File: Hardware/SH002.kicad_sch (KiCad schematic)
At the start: 11 parts, among them J3 Conn_01x04, J5 Conn_01x04, J7 Conn_01x04

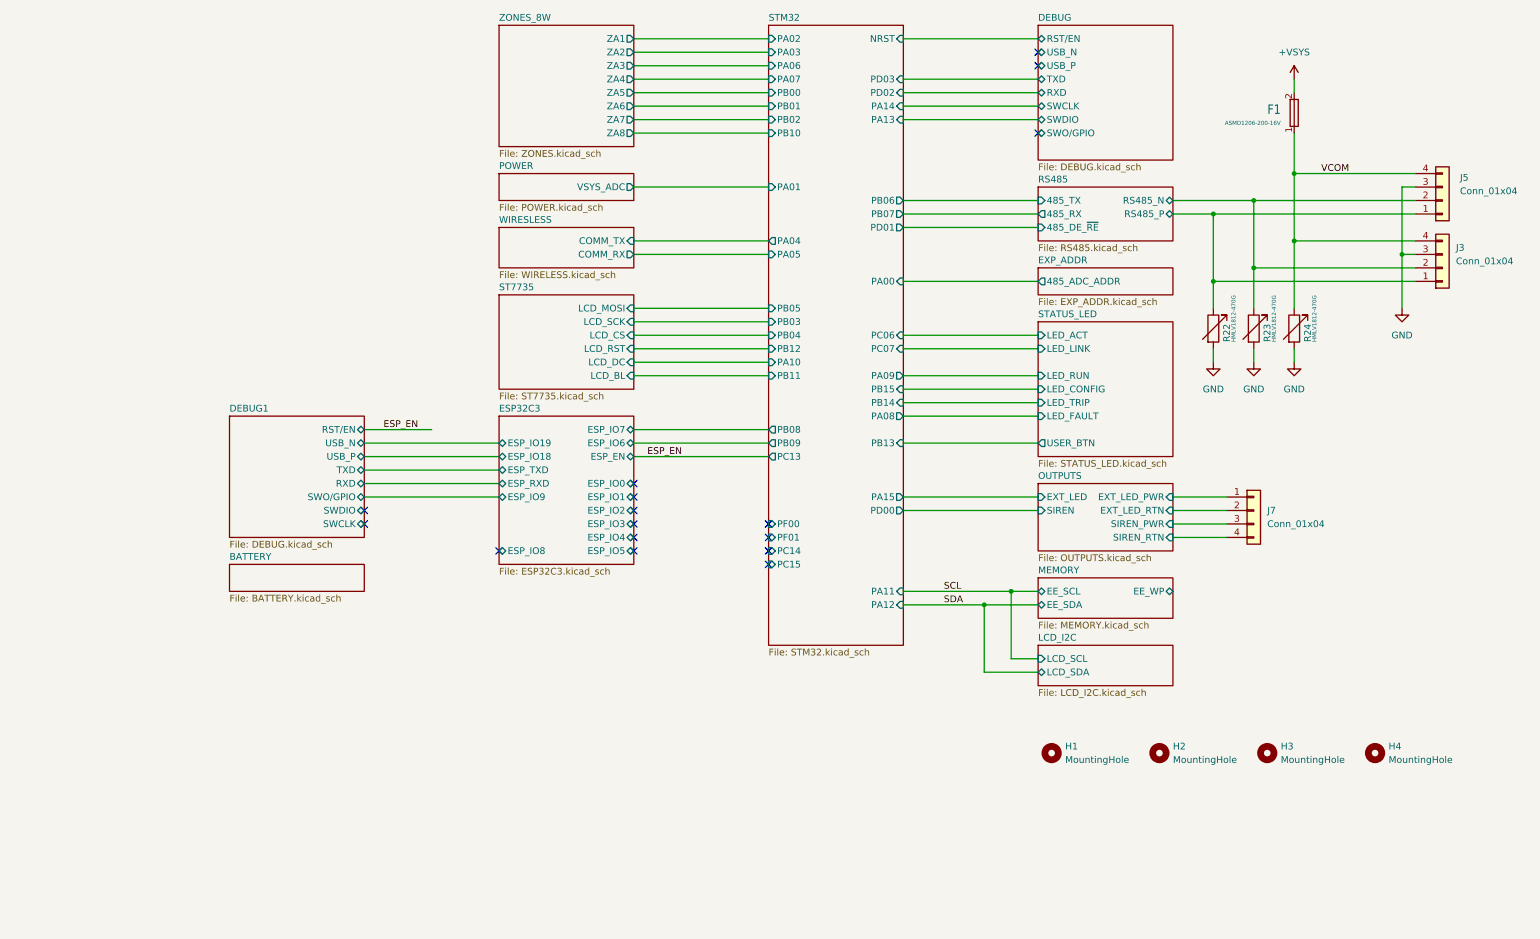
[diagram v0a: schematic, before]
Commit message: remove unused sheets
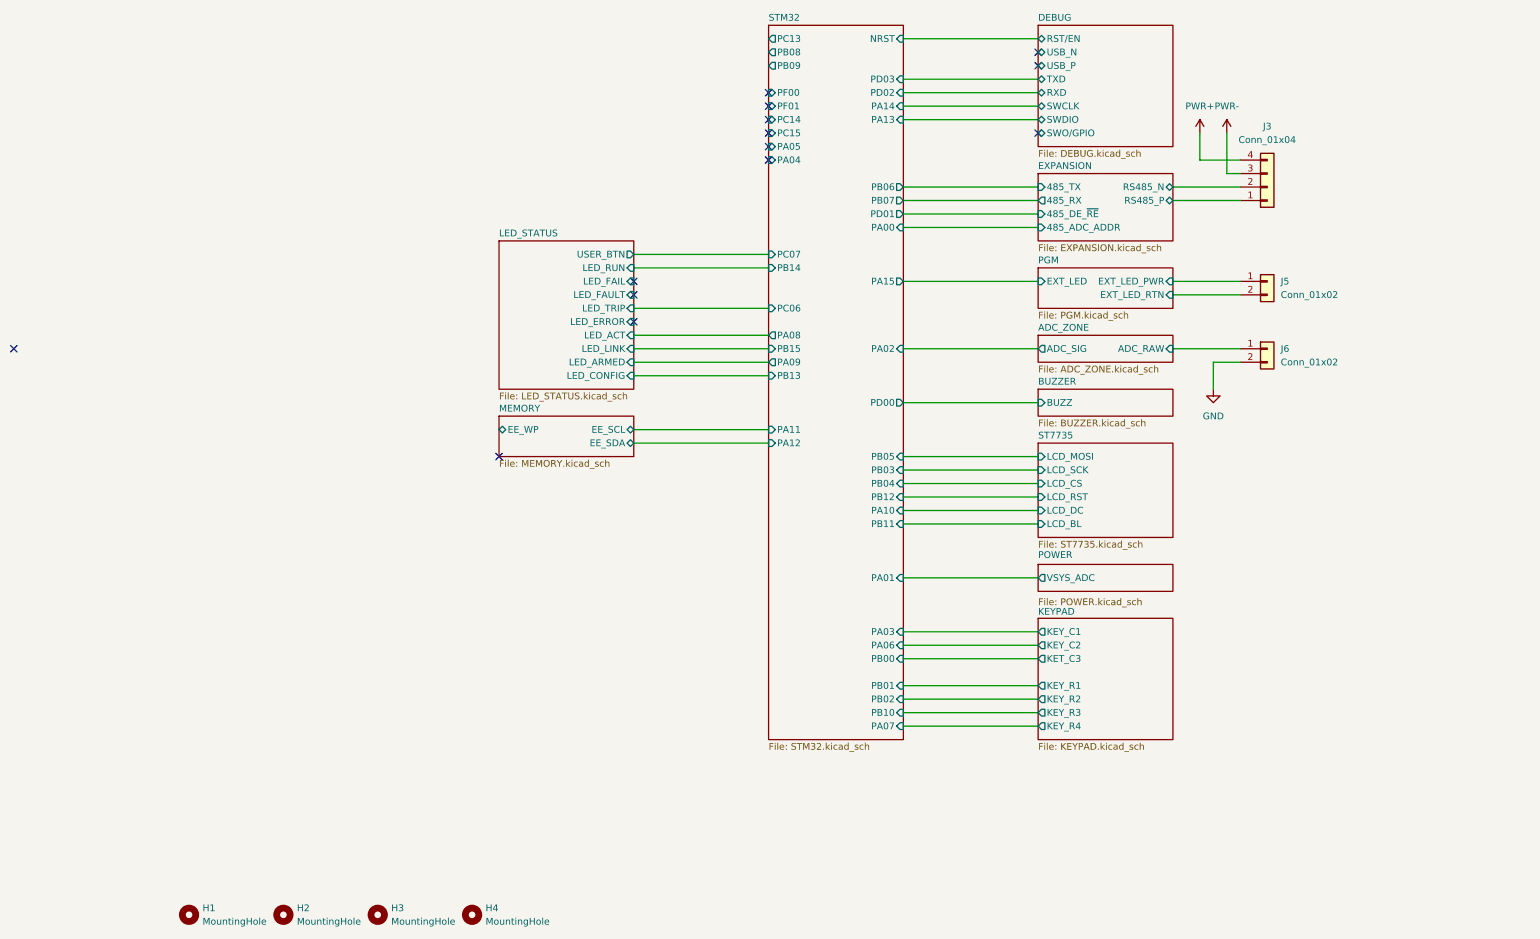
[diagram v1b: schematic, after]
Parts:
- removed F1: ASMD1206-200-16V, EasyEDA:F1206, symbol PCM_JLCPCB-Extended:Fuse, ASMD1206-200-16V
- removed J5, J7: Conn_01x04, EASYEDA2KICAD:PhoenixContact_MC_1,5_4-G-3.81_1x04_P3.81mm_Horizontal, symbol Connector_Generic:Conn_01x04
- removed R22, R23, R24: HMLV1812-470G, Resistor_SMD:R_1812_4532Metric_Pad1.30x3.40mm_HandSolder, symbol PCM_JLCPCB-Extended:MOV, HMLV1812-470G
- added J5, J6: Conn_01x02, EASYEDA2KICAD:PhoenixContact_MC_1,5_2-G-3.81_1x02_P3.81mm_Horizontal, symbol Connector_Generic:Conn_01x02
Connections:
- net GND: now also J6.2 (Pin_2); no longer J3.3 (Pin_3)
- net RS485/RS485_N renamed EXPANSION/RS485_N
- net RS485/RS485_P renamed EXPANSION/RS485_P
- net VCOM renamed PWR+
- new net ADC_ZONE/ADC_RAW: J6.1 (Pin_1)
- new net PGM/EXT_LED_PWR: J5.1 (Pin_1)
- new net PGM/EXT_LED_RTN: J5.2 (Pin_2)
- new net PWR-: J3.3 (Pin_3)
- no-connect marks 16 -> 14
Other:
- removed sheet BATTERY
- removed sheet DEBUG1
- removed sheet ESP32C3
- removed sheet EXP_ADDR
- removed sheet LCD_I2C
- removed sheet OUTPUTS
- removed sheet RS485
- removed sheet STATUS_LED
- removed sheet WIRESLESS
- removed sheet ZONES_8W
- added sheet ADC_ZONE (ADC_ZONE.kicad_sch)
- added sheet BUZZER (BUZZER.kicad_sch)
- added sheet EXPANSION (EXPANSION.kicad_sch)
- added sheet KEYPAD (KEYPAD.kicad_sch)
- added sheet LED_STATUS (LED_STATUS.kicad_sch)
- added sheet PGM (PGM.kicad_sch)
